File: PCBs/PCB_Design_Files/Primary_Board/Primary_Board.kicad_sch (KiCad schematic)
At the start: 6 parts, among them J3 5034801000, J4 Conn_01x10_Pin

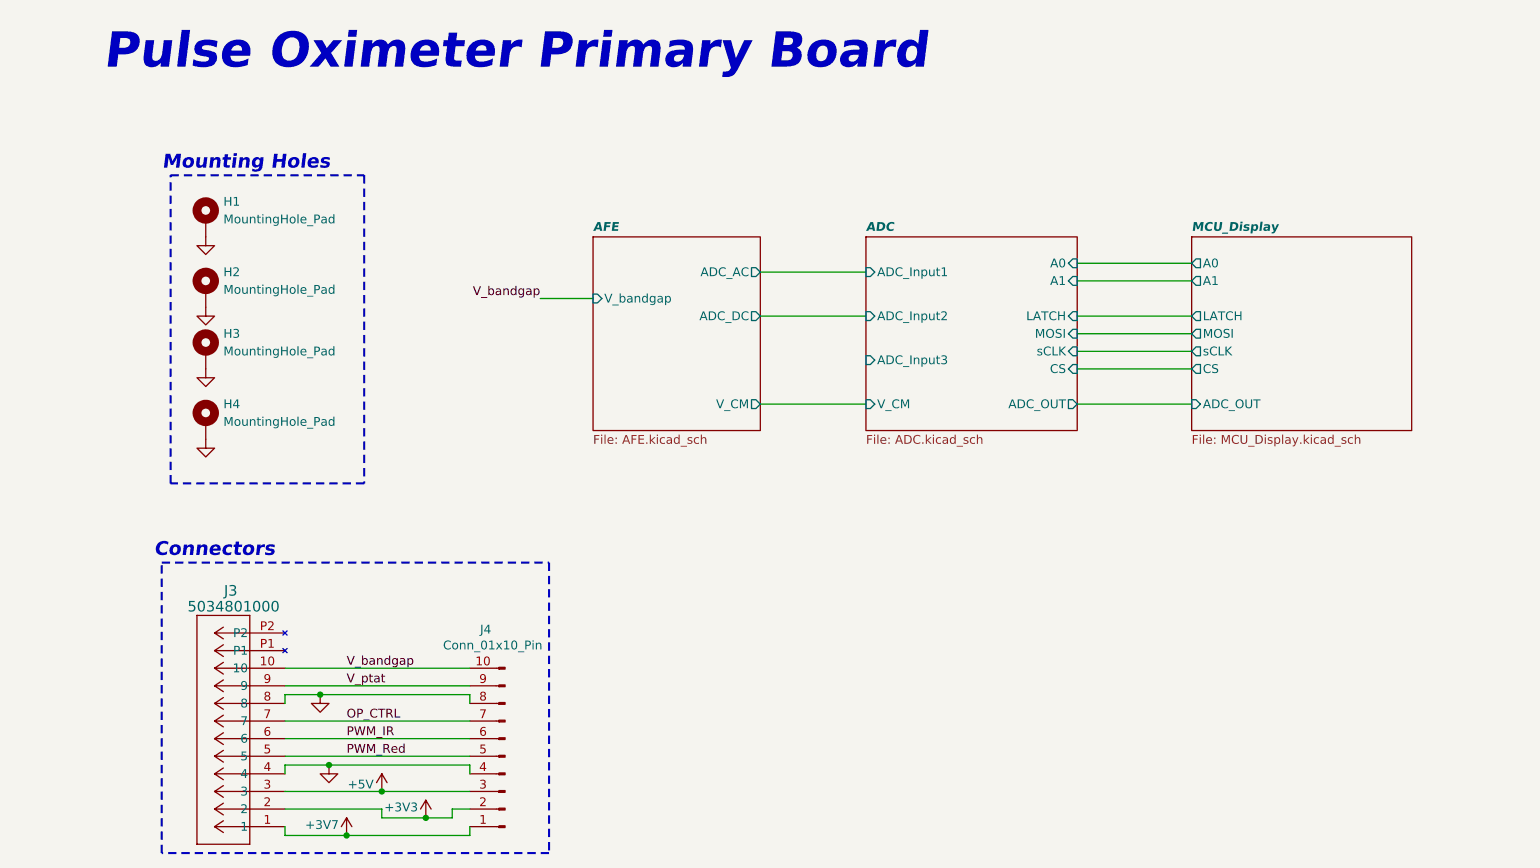
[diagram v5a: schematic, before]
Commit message: updated mcu pins
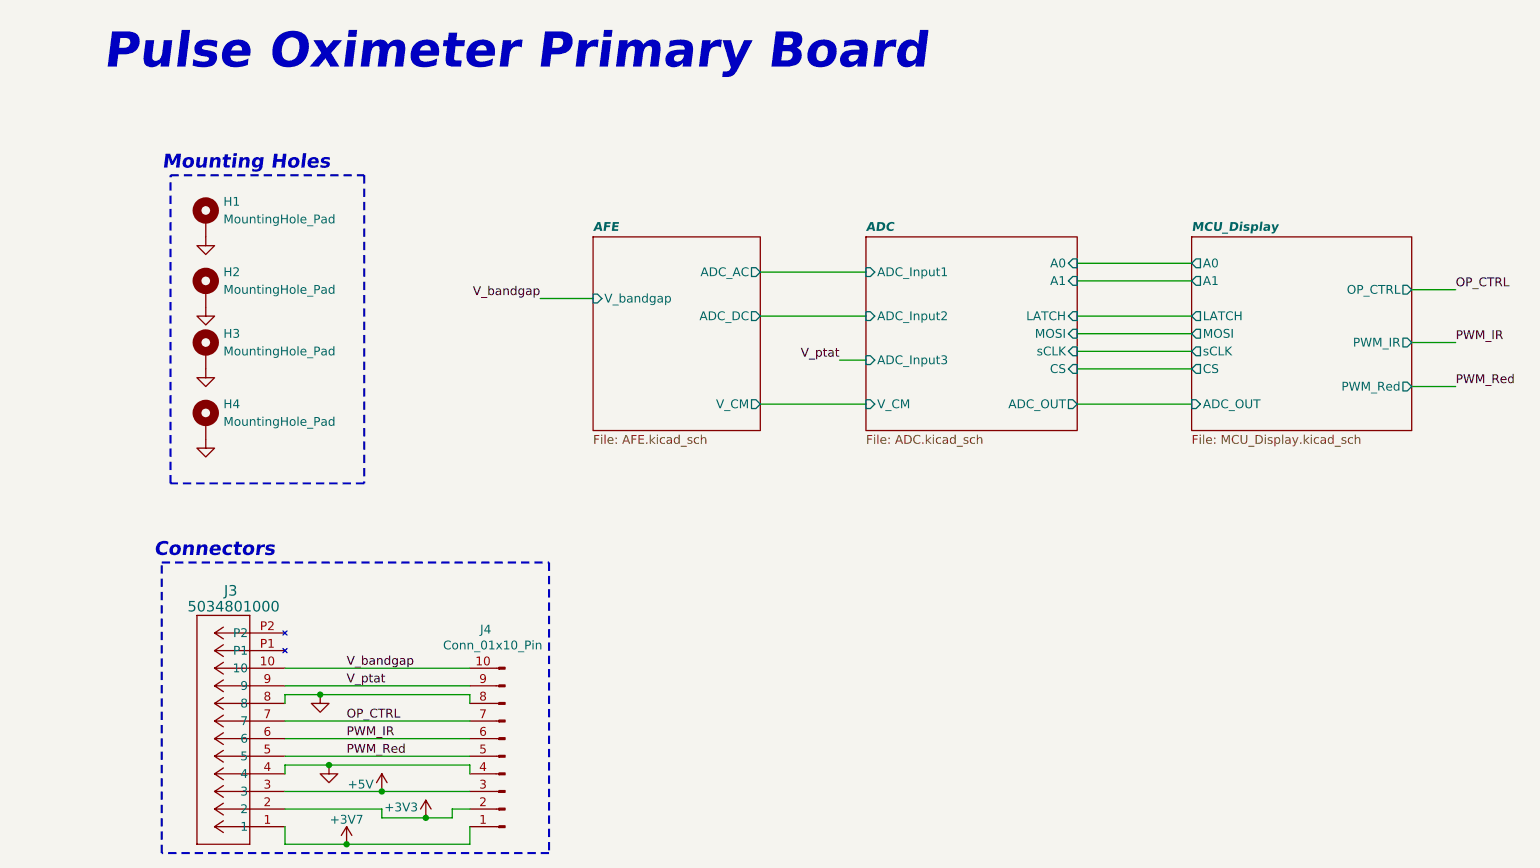
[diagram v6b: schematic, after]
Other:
- sheet MCU_Display ports: added OP_CTRL, PWM_IR, PWM_Red; removed none
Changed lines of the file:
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@@
 	)
 	(junction
-		(at 50.8 133.35)
+		(at 50.8 134.62)
 		(diameter 0)
 		(color 0 0 0 0)
@@
 	(wire
 		(pts
+			(xy 121.92 64.77) (xy 125.73 64.77)
+		)
+		(stroke
+			(width 0)
+			(type default)
+		)
+	)
+	(wire
+		(pts
 			(xy 156.21 53.34) (xy 172.72 53.34)
 		)
@@
 	(wire
 		(pts
+			(xy 204.47 68.58) (xy 210.82 68.58)
+		)
+		(stroke
+			(width 0)
+			(type default)
+		)
+	)
+	(wire
+		(pts
 			(xy 156.21 63.5) (xy 172.72 63.5)
 		)
@@
 	(wire
 		(pts
+			(xy 50.8 134.62) (xy 68.58 134.62)
+		)
+		(stroke
+			(width 0)
+			(type default)
+		)
+	)
+	(wire
+		(pts
 			(xy 156.21 58.42) (xy 172.72 58.42)
 		)
@@
 	(wire
 		(pts
-			(xy 41.91 133.35) (xy 41.91 132.08)
+			(xy 41.91 134.62) (xy 41.91 132.08)
 		)
 		(stroke
@@
 	(wire
 		(pts
-			(xy 68.58 133.35) (xy 68.58 132.08)
+			(xy 68.58 134.62) (xy 68.58 132.08)
 		)
 		(stroke
@@
 	(wire
 		(pts
-			(xy 41.91 133.35) (xy 50.8 133.35)
+			(xy 41.91 134.62) (xy 50.8 134.62)
 		)
 		(stroke
@@
 	(wire
 		(pts
-			(xy 50.8 133.35) (xy 68.58 133.35)
-		)
-		(stroke
-			(width 0)
-			(type default)
-		)
-	)
-	(wire
-		(pts
 			(xy 62.23 130.81) (xy 66.04 130.81)
 		)
@@
 	(wire
 		(pts
+			(xy 204.47 54.61) (xy 210.82 54.61)
+		)
+		(stroke
+			(width 0)
+			(type default)
+		)
+	)
+	(wire
+		(pts
 			(xy 156.21 66.04) (xy 172.72 66.04)
+		)
+		(stroke
+			(width 0)
+			(type default)
+		)
+	)
+	(wire
+		(pts
+			(xy 204.47 62.23) (xy 210.82 62.23)
 		)
 		(stroke
@@
 		)
 	)
+	(label "OP_CTRL"
+		(at 210.82 54.61 0)
+		(effects
+			(font
+				(size 1.27 1.27)
+			)
+			(justify left bottom)
+		)
+	)
 	(label "V_bandgap"
 		(at 78.74 55.88 180)
@@
 		)
 	)
+	(label "PWM_Red"
+		(at 210.82 68.58 0)
+		(effects
+			(font
+				(size 1.27 1.27)
+			)
+			(justify left bottom)
+		)
+	)
+	(label "V_ptat"
+		(at 121.92 64.77 180)
+		(effects
+			(font
+				(size 1.27 1.27)
+			)
+			(justify right bottom)
+		)
+	)
 	(label "OP_CTRL"
 		(at 50.8 116.84 0)
+		(effects
+			(font
+				(size 1.27 1.27)
+			)
+			(justify left bottom)
+		)
+	)
+	(label "PWM_IR"
+		(at 210.82 62.23 0)
 		(effects
 			(font
@@
 	)
 	(symbol
+		(lib_id "power:+3V8")
+		(at 50.8 134.62 0)
+		(unit 1)
+		(exclude_from_sim no)
+		(in_bom yes)
+		(on_board yes)
+		(dnp no)
+		(property "Reference" "#PWR071"
+			(at 50.8 138.43 0)
+			(effects
+				(font
+					(size 1.27 1.27)
+				)
+				(hide yes)
+			)
+		)
+		(property "Value" "+3V7"
+			(at 50.8 131.064 0)
+			(effects
+				(font
+					(size 1.27 1.27)
+				)
+			)
+		)
+		(property "Footprint" ""
+			(at 50.8 134.62 0)
+			(effects
+				(font
+					(size 1.27 1.27)
+				)
+				(hide yes)
+			)
+		)
+		(property "Datasheet" ""
+			(at 50.8 134.62 0)
+			(effects
+				(font
+					(size 1.27 1.27)
+				)
+				(hide yes)
+			)
+		)
+		(property "Description" "Power symbol creates a global label with name \"+3V8\""
+			(at 50.8 134.62 0)
+			(effects
+				(font
+					(size 1.27 1.27)
+				)
+				(hide yes)
+			)
+		)
+		(pin "1"
+		)
+		(instances
+			(project "Primary_Board"
+				(path "/8c3d01e8-a984-4e4e-9220-7d351336a99b"
+					(reference "#PWR071")
+					(unit 1)
+				)
+			)
+		)
+	)
+	(symbol
 		(lib_id "Connector:Conn_01x10_Pin")
 		(at 73.66 121.92 180)
@@
 	(symbol
 		(lib_id "power:+3V3")
-		(at 50.8 133.35 0)
-		(unit 1)
-		(exclude_from_sim no)
-		(in_bom yes)
-		(on_board yes)
-		(dnp no)
-		(property "Reference" "#PWR071"
-			(at 50.8 137.16 0)
-			(effects
-				(font
-					(size 1.27 1.27)
-				)
-				(hide yes)
-			)
-		)
-		(property "Value" "+3V7"
-			(at 47.244 131.826 0)
-			(effects
-				(font
-					(size 1.27 1.27)
-				)
-			)
-		)
-		(property "Footprint" ""
-			(at 50.8 133.35 0)
-			(effects
-				(font
-					(size 1.27 1.27)
-				)
-				(hide yes)
-			)
-		)
-		(property "Datasheet" ""
-			(at 50.8 133.35 0)
-			(effects
-				(font
-					(size 1.27 1.27)
-				)
-				(hide yes)
-			)
-		)
-		(property "Description" "Power symbol creates a global label with name \"+3V3\""
-			(at 50.8 133.35 0)
-			(effects
-				(font
-					(size 1.27 1.27)
-				)
-				(hide yes)
-			)
-		)
-		(pin "1"
-		)
-		(instances
-			(project "Primary_Board"
-				(path "/8c3d01e8-a984-4e4e-9220-7d351336a99b"
-					(reference "#PWR071")
-					(unit 1)
-				)
-			)
-		)
-	)
-	(symbol
-		(lib_id "power:+3V3")
 		(at 62.23 130.81 0)
 		(unit 1)
@@
 			)
 		)
+		(pin "OP_CTRL" output
+			(at 204.47 54.61 0)
+			(effects
+				(font
+					(size 1.27 1.27)
+				)
+				(justify right)
+			)
+		)
+		(pin "PWM_IR" output
+			(at 204.47 62.23 0)
+			(effects
+				(font
+					(size 1.27 1.27)
+				)
+				(justify right)
+			)
+		)
+		(pin "PWM_Red" output
+			(at 204.47 68.58 0)
+			(effects
+				(font
+					(size 1.27 1.27)
+				)
+				(justify right)
+			)
+		)

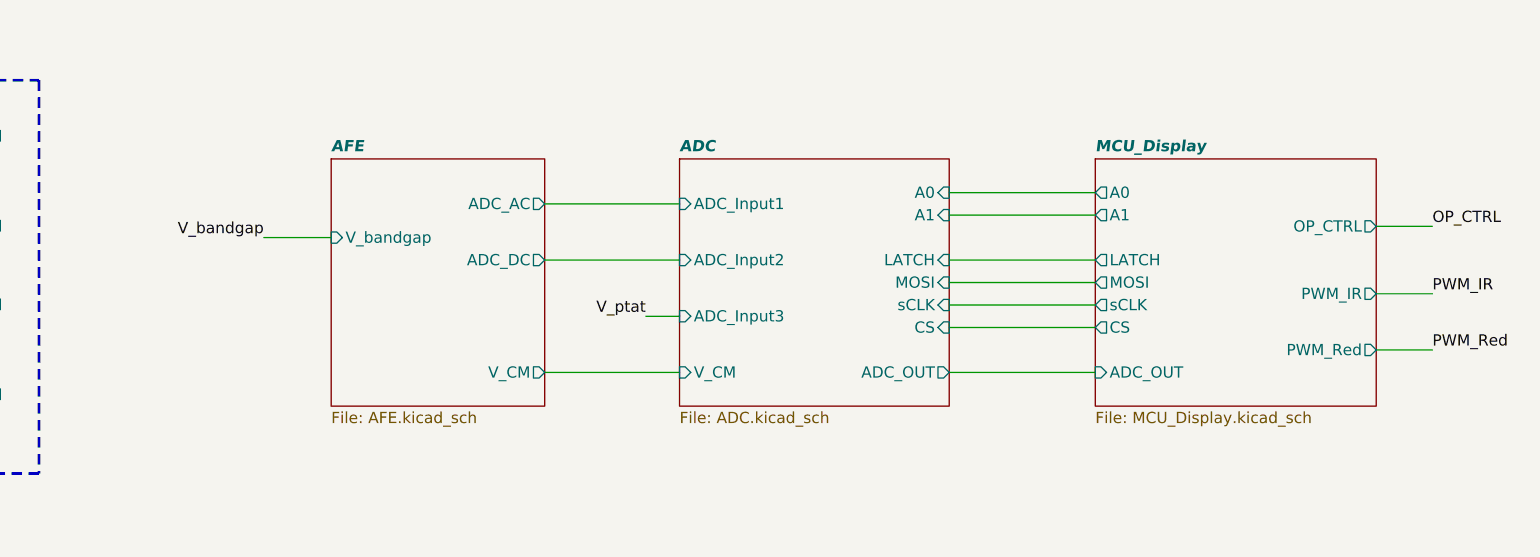
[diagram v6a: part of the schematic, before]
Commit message: routed LED driver gpio on primary board
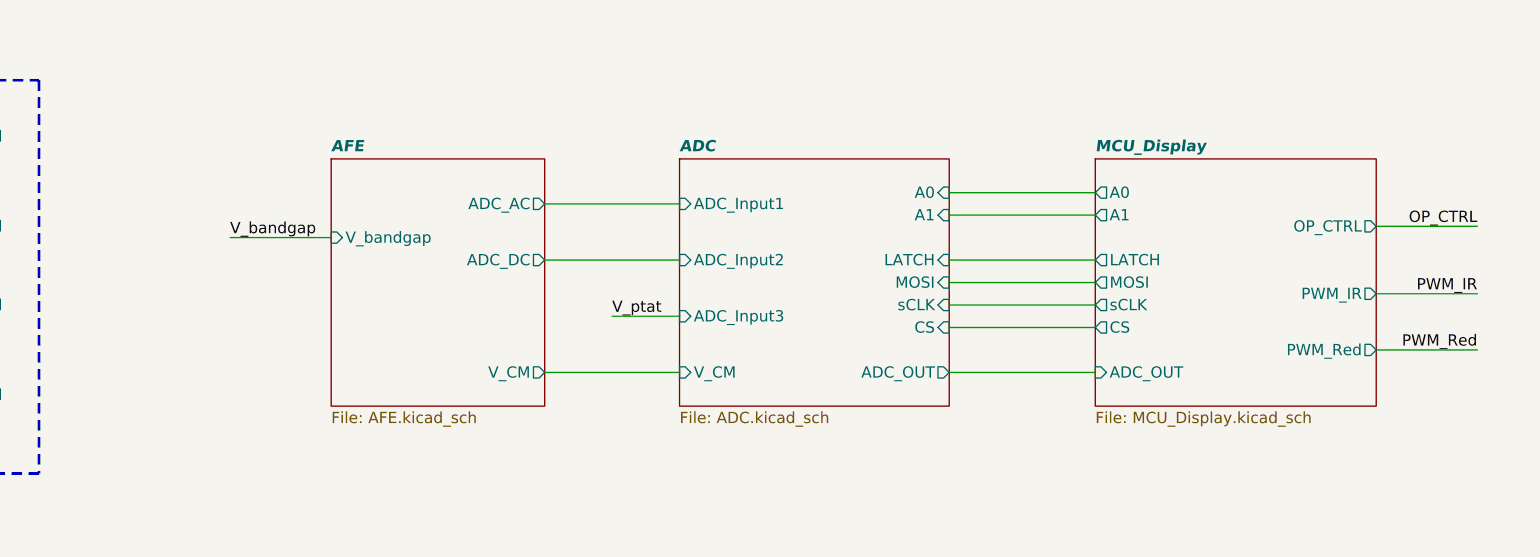
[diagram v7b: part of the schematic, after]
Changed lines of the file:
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@@
 	(wire
 		(pts
-			(xy 78.74 55.88) (xy 86.36 55.88)
+			(xy 74.93 55.88) (xy 86.36 55.88)
 		)
 		(stroke
@@
 	(wire
 		(pts
-			(xy 121.92 64.77) (xy 125.73 64.77)
+			(xy 118.11 64.77) (xy 125.73 64.77)
 		)
 		(stroke
@@
 	(wire
 		(pts
-			(xy 204.47 68.58) (xy 210.82 68.58)
+			(xy 204.47 68.58) (xy 215.9 68.58)
 		)
 		(stroke
@@
 	(wire
 		(pts
-			(xy 204.47 54.61) (xy 210.82 54.61)
+			(xy 204.47 54.61) (xy 215.9 54.61)
 		)
 		(stroke
@@
 	(wire
 		(pts
-			(xy 204.47 62.23) (xy 210.82 62.23)
+			(xy 204.47 62.23) (xy 215.9 62.23)
 		)
 		(stroke
@@
 	)
 	(label "OP_CTRL"
-		(at 210.82 54.61 0)
-		(effects
-			(font
-				(size 1.27 1.27)
-			)
-			(justify left bottom)
+		(at 215.9 54.61 180)
+		(effects
+			(font
+				(size 1.27 1.27)
+			)
+			(justify right bottom)
 		)
 	)
 	(label "V_bandgap"
-		(at 78.74 55.88 180)
+		(at 74.93 55.88 0)
+		(effects
+			(font
+				(size 1.27 1.27)
+			)
+			(justify left bottom)
+		)
+	)
+	(label "PWM_Red"
+		(at 215.9 68.58 180)
 		(effects
 			(font
@@
 		)
 	)
-	(label "PWM_Red"
-		(at 210.82 68.58 0)
-		(effects
-			(font
-				(size 1.27 1.27)
-			)
-			(justify left bottom)
-		)
-	)
 	(label "V_ptat"
-		(at 121.92 64.77 180)
-		(effects
-			(font
-				(size 1.27 1.27)
-			)
-			(justify right bottom)
+		(at 118.11 64.77 0)
+		(effects
+			(font
+				(size 1.27 1.27)
+			)
+			(justify left bottom)
 		)
 	)
@@
 	)
 	(label "PWM_IR"
-		(at 210.82 62.23 0)
-		(effects
-			(font
-				(size 1.27 1.27)
-			)
-			(justify left bottom)
-		)
-	)
+		(at 215.9 62.23 180)
+		(effects
+			(font
+				(size 1.27 1.27)
+			)
+			(justify right bottom)
+		)
+	)
